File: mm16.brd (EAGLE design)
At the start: 100 x 80 mm, 54 parts, among them IC101 ATMEGA32-PU, IC102 DS1337, IC103 MAX483CPA, IC201 LTV847, IC202 LTV847, IC203 LTV847, IC204 LTV847, Q1 32,768kHz

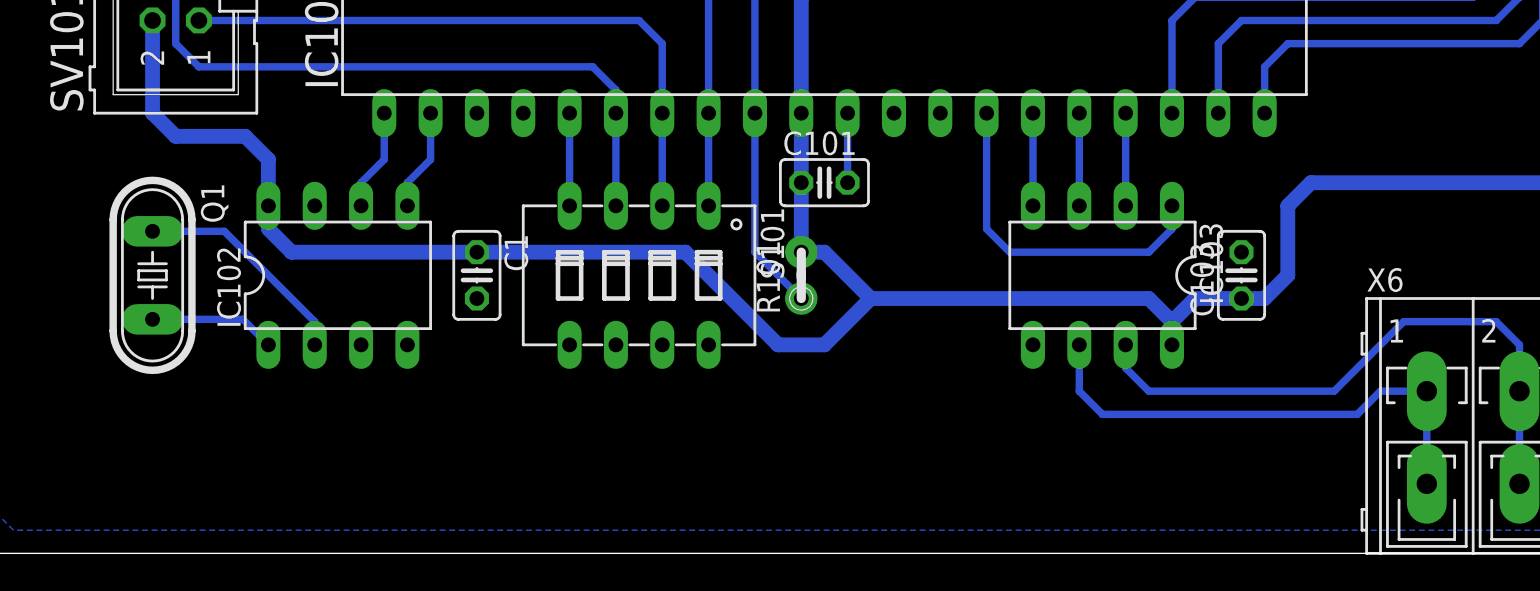
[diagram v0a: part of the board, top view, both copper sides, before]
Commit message: Batterie auf Multimaster hinzugefügt
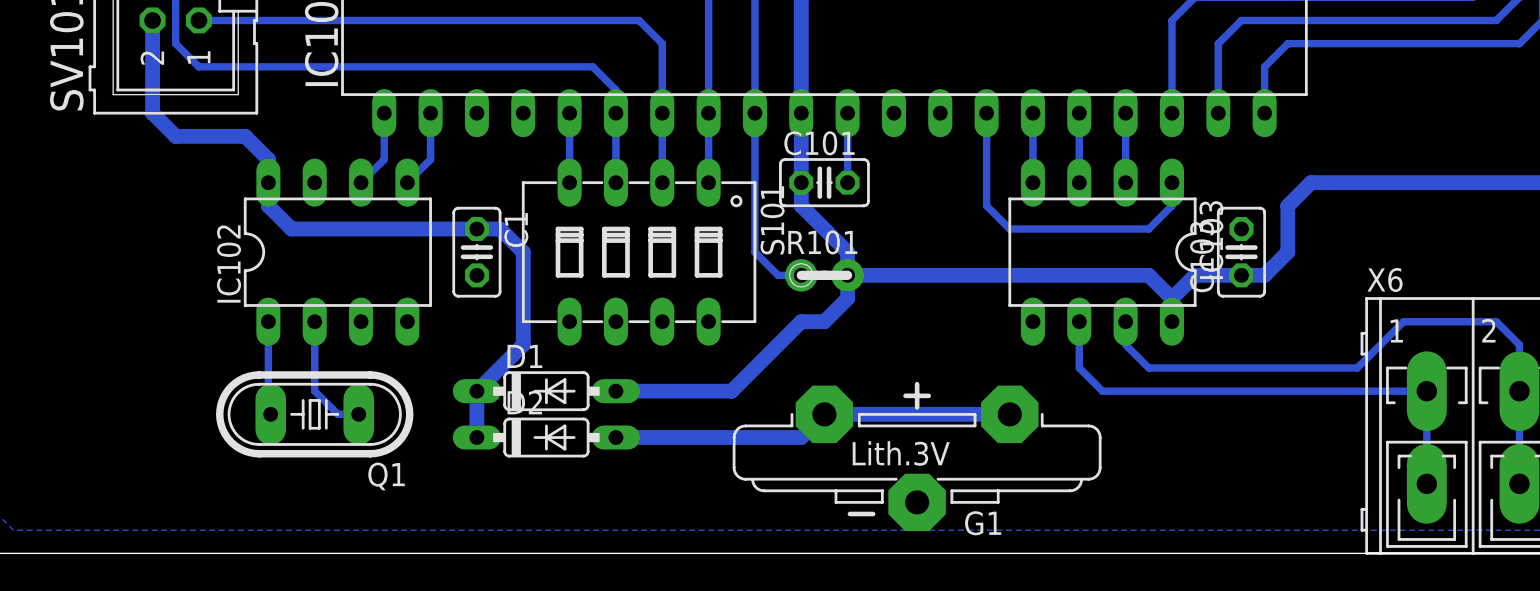
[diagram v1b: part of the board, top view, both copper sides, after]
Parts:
- added D1, D2: 1N4148-7, diode:DO35-7
- added G1: CR2032V, battery:CR2032V
- moved Q1 11.7 mm to (19.1, 7.62), turned to 180 degrees
- moved R101 1.27 mm to (47.0, 15.2), turned to 0 degrees
- moved C1 1.27 mm to (27.9, 16.5)
- moved C103 1.27 mm to (69.8, 16.5)
- moved IC102 1.27 mm to (20.3, 16.5)
- moved IC103 1.27 mm to (62.2, 16.5)
- moved S101 1.27 mm to (36.8, 16.5)
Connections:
- new net N$21: D2.A, G1.+, G1.+@1
- new net VCC: C1.1, D1.C, D2.C, IC102.8, SV101.VCC
- net +5V: now also D1.A; no longer C1.1, IC102.8, SV101.VCC
- net GND: now also G1.-
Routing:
- net VCC: track 0.00 -> 41.3 mm
- net +5V: track 193.7 -> 154.2 mm
- net N$21: track 0.00 -> 22.1 mm
- net N$127: track 12.2 -> 6.75 mm
- net N$126: track 6.93 -> 5.13 mm
- net N$62: track 18.8 -> 17.6 mm
- net N$123: track 34.8 -> 33.5 mm
- net N$122: track 35.9 -> 34.6 mm
- net SDA: track 5.61 -> 4.34 mm
- net SCL: track 5.61 -> 4.34 mm
- net N$64: track 5.08 -> 3.81 mm
- net N$63: track 5.08 -> 3.81 mm
- net N$61: track 5.08 -> 3.81 mm
- net N$130: track 5.08 -> 3.81 mm
- net N$125: track 39.9 -> 38.6 mm
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
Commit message: Dipschalter durch Drehschalter ersetzt; 74HC594 durch 74HC595 ersetzt; Signalleitungen gedreht.
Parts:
- removed S101: (no value), schalter:DIP04YL
- added S1: (no value), switch-dil:P103
- moved D1 1.27 mm to (31.8, 7.62)
- moved D2 1.27 mm to (31.8, 5.08)
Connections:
- net !R: now also X1.5, X1.6; no longer X1.10, X1.9
- net C1: now also X1.7, X1.8; no longer X1.5, X1.6
- net C2: now also X1.10, X1.9; no longer X1.7, X1.8
- net GND: now also S1.C; no longer S101.5, S101.6, S101.7, S101.8
- net N$122: now also S1.8; no longer S101.3
- net N$123: now also S1.2; no longer S101.2
- net N$125: now also S1.4; no longer S101.1
- net N$130: now also S1.1; no longer S101.4
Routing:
- net N$130: track 3.81 -> 13.0 mm
- net N$125: track 38.6 -> 47.8 mm
- net !R: track 29.0 -> 38.0 mm
- net +5V: track 154.2 -> 151.5 mm
- net C2: track 39.5 -> 36.9 mm
- net C1: track 43.8 -> 41.3 mm
- net VCC: track 41.3 -> 42.5 mm
- net N$122: track 34.6 -> 35.1 mm
- net N$21: track 22.1 -> 22.6 mm
- net N$123: track 33.5 -> 34.1 mm

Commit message: Leiterbahn verschoben
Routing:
- net +5V: track 151.5 -> 152.2 mm
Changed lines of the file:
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@@
 <layer number="43" name="vRestrict" color="2" fill="10" visible="yes" active="yes"/>
 <layer number="44" name="Drills" color="7" fill="1" visible="no" active="yes"/>
-<layer number="45" name="Holes" color="7" fill="1" visible="no" active="yes"/>
+<layer number="45" name="Holes" color="7" fill="1" visible="yes" active="yes"/>
 <layer number="46" name="Milling" color="3" fill="1" visible="no" active="yes"/>
 <layer number="47" name="Measures" color="7" fill="1" visible="no" active="yes"/>
@@
 <wire x1="100" y1="80" x2="0" y2="80" width="0" layer="20"/>
 <wire x1="0" y1="80" x2="0" y2="0" width="0" layer="20"/>
+<hole x="7.62" y="19.05" drill="5"/>
+<hole x="82.55" y="19.05" drill="5"/>
 </plain>
 <attributes>
@@
 <wire x1="96.52" y1="46.99" x2="93.98" y2="46.99" width="0.8128" layer="16"/>
 <wire x1="93.98" y1="44.45" x2="93.98" y2="46.99" width="0.8128" layer="16"/>
-<wire x1="69.85" y1="15.24" x2="71.12" y2="15.24" width="0.8128" layer="16"/>
-<wire x1="71.12" y1="15.24" x2="72.39" y2="16.51" width="0.8128" layer="16"/>
-<wire x1="72.39" y1="16.51" x2="72.39" y2="19.05" width="0.8128" layer="16"/>
-<wire x1="72.39" y1="19.05" x2="73.66" y2="20.32" width="0.8128" layer="16"/>
-<wire x1="73.66" y1="20.32" x2="90.17" y2="20.32" width="0.8128" layer="16"/>
+<wire x1="69.85" y1="15.24" x2="88.9" y2="15.24" width="0.8128" layer="16"/>
+<wire x1="88.9" y1="15.24" x2="90.17" y2="16.51" width="0.8128" layer="16"/>
+<wire x1="90.17" y1="16.51" x2="90.17" y2="20.32" width="0.8128" layer="16"/>
 <wire x1="93.98" y1="44.45" x2="92.71" y2="44.45" width="0.8128" layer="16"/>
 <wire x1="92.71" y1="44.45" x2="83.82" y2="35.56" width="0.8128" layer="16"/>
@@
 <wire x1="48.26" y1="16.51" x2="48.26" y2="15.24" width="0.8128" layer="16"/>
 <wire x1="48.26" y1="15.24" x2="48.26" y2="13.97" width="0.8128" layer="16"/>
-<wire x1="48.26" y1="13.97" x2="46.99" y2="12.7" width="0.8128" layer="16"/>
-<wire x1="46.99" y1="12.7" x2="45.72" y2="12.7" width="0.8128" layer="16"/>
-<wire x1="45.72" y1="12.7" x2="40.64" y2="7.62" width="0.8128" layer="16"/>
+<wire x1="48.26" y1="13.97" x2="45.72" y2="11.43" width="0.8128" layer="16"/>
+<wire x1="45.72" y1="11.43" x2="44.45" y2="11.43" width="0.8128" layer="16"/>
+<wire x1="44.45" y1="11.43" x2="40.64" y2="7.62" width="0.8128" layer="16"/>
 </signal>
 <signal name="N$42">
@@
 <contactref element="IC101" pad="1"/>
 <contactref element="IC102" pad="6"/>
-<wire x1="21.59" y1="20.32" x2="22.86" y2="21.59" width="0.4064" layer="16"/>
-<wire x1="22.86" y1="21.59" x2="22.86" y2="24.13" width="0.4064" layer="16"/>
+<wire x1="21.59" y1="20.32" x2="21.59" y2="21.59" width="0.4064" layer="16"/>
+<wire x1="21.59" y1="21.59" x2="22.86" y2="22.86" width="0.4064" layer="16"/>
+<wire x1="22.86" y1="22.86" x2="22.86" y2="24.13" width="0.4064" layer="16"/>
 </signal>
 <signal name="SDA">
 <contactref element="IC101" pad="2"/>
 <contactref element="IC102" pad="5"/>
-<wire x1="24.13" y1="20.32" x2="25.4" y2="21.59" width="0.4064" layer="16"/>
-<wire x1="25.4" y1="21.59" x2="25.4" y2="24.13" width="0.4064" layer="16"/>
+<wire x1="24.13" y1="20.32" x2="24.13" y2="21.59" width="0.4064" layer="16"/>
+<wire x1="24.13" y1="21.59" x2="25.4" y2="22.86" width="0.4064" layer="16"/>
+<wire x1="25.4" y1="22.86" x2="25.4" y2="24.13" width="0.4064" layer="16"/>
 </signal>
 <signal name="N$126">

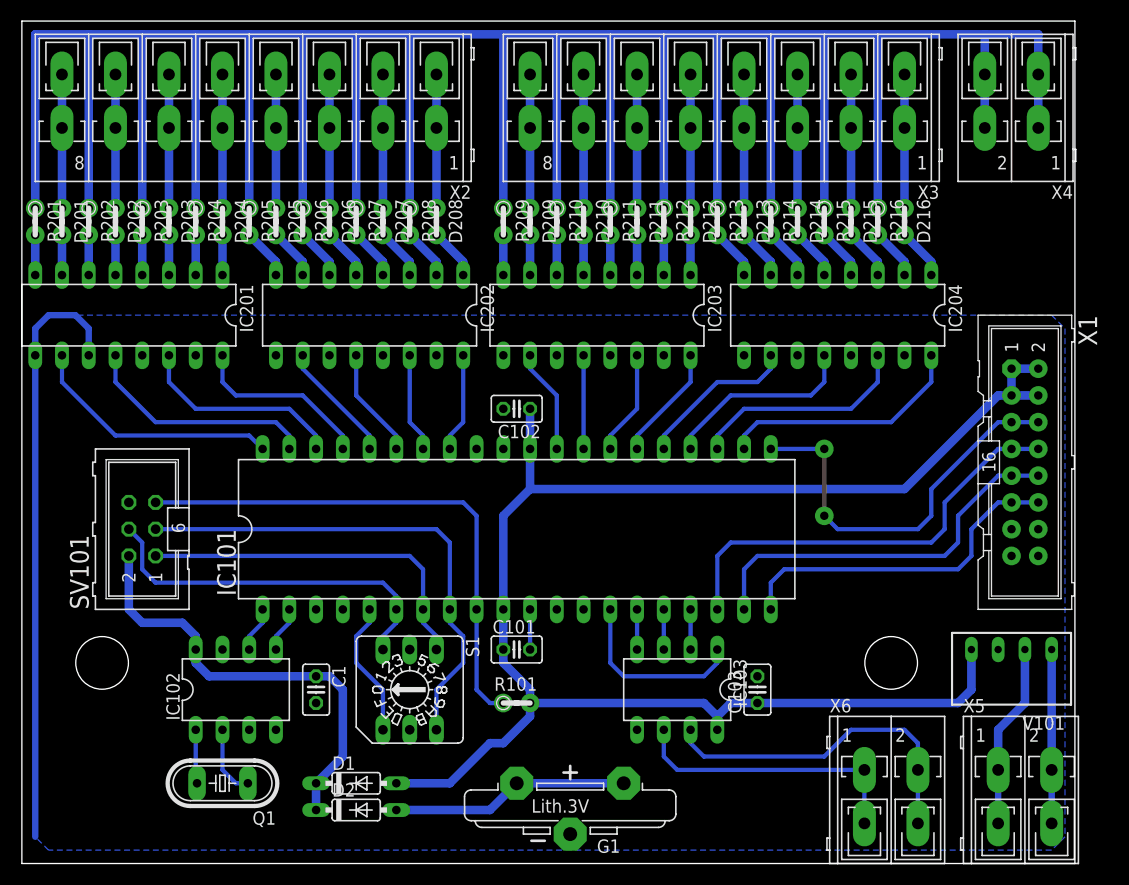
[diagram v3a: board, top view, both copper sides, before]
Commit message: Boards beschriftet
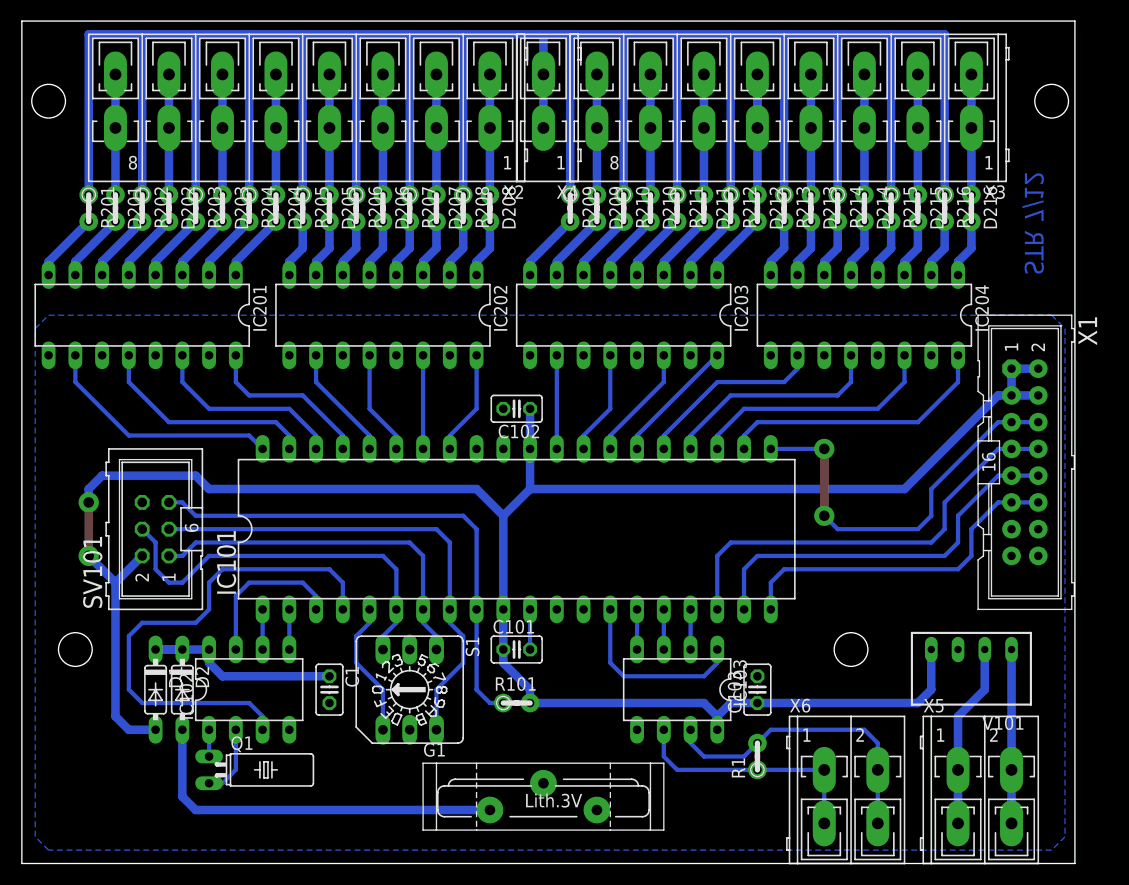
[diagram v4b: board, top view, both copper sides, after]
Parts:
- added R1: 120Ω, passiv:0204V
- C1, C101, C102, C103: value 10nF -> 100nF
- G1: value CR2032V -> KZH20PCB-V; device battery:CR2032V -> batterie:KZH20PCB-V
- Q1: device passiv:HC49/S -> passiv:TC38H
- R201, R202, R203, R204, R205, R206, R207, R208, R209, R210, R211, R212, R213, R214, R215, R216: value (none) -> 220kΩ
- X4: device anschluss:WAGO_236-402 -> anschluss:WAGO_236-401
- moved X4 44.5 mm to (49.5, 71.1)
- moved D1 21.0 mm to (12.7, 16.5), turned to 270 degrees
- moved D2 20.1 mm to (15.2, 16.5), turned to 270 degrees
- moved D213 6.48 mm to (74.9, 62.2)
- moved D214 6.48 mm to (80.0, 62.2)
- moved D215 6.48 mm to (85.1, 62.2)
- moved D216 6.48 mm to (90.2, 62.2)
- moved D209 6.48 mm to (54.6, 62.2)
- moved R209 6.48 mm to (52.1, 62.2)
- moved R210 6.48 mm to (57.1, 62.2)
- moved R212 6.48 mm to (67.3, 62.2)
- moved D210 6.48 mm to (59.7, 62.2)
- moved D211 6.48 mm to (64.8, 62.2)
- moved D212 6.48 mm to (69.8, 62.2)
- moved R211 6.48 mm to (62.2, 62.2)
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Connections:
- removed net N$19: IC103.7, X6.A2, X6.B2
- new net ALARM1: IC101.4, IC102.3
- new net ALARM2: IC101.3, IC102.7
- new net N$22: IC103.7, R1.2, X6.A2, X6.B2
- net +5V: now also SV101.VCC
- net GNDIO: no longer X4.A2, X4.B2
- net N$126: now also Q1.1; no longer Q1.2
- net N$127: now also Q1.2; no longer Q1.1
- net N$20: now also R1.1
- net N$21: now also G1.+1, G1.+2; no longer G1.+, G1.+@1
- net VCC: no longer SV101.VCC
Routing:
- net GND: track 60.7 -> 3.81 mm
- net +5V: track 152.2 -> 203.9 mm, vias 0 -> 2
- net ALARM1: track 0.00 -> 47.6 mm
- net GNDIO: track 377.2 -> 334.0 mm
- net N$19: track 32.6 -> 0.00 mm
- net N$22: track 0.00 -> 28.8 mm
- net VCC: track 42.5 -> 20.8 mm
- net ALARM2: track 0.00 -> 15.0 mm
- net N$21: track 22.6 -> 36.1 mm
- net N$83: track 12.7 -> 16.5 mm
- net N$20: track 27.2 -> 23.4 mm
- net N$6: track 3.81 -> 6.66 mm
- net N$32: track 3.81 -> 6.66 mm
- net N$26: track 3.81 -> 6.66 mm
- net N$25: track 3.81 -> 6.66 mm
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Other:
- board text added: "STR 7/12"
